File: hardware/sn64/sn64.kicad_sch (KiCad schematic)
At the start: 2 parts, among them J1 N64_Cartridge_Edge_50, J2 SNES_Female_Slot_62

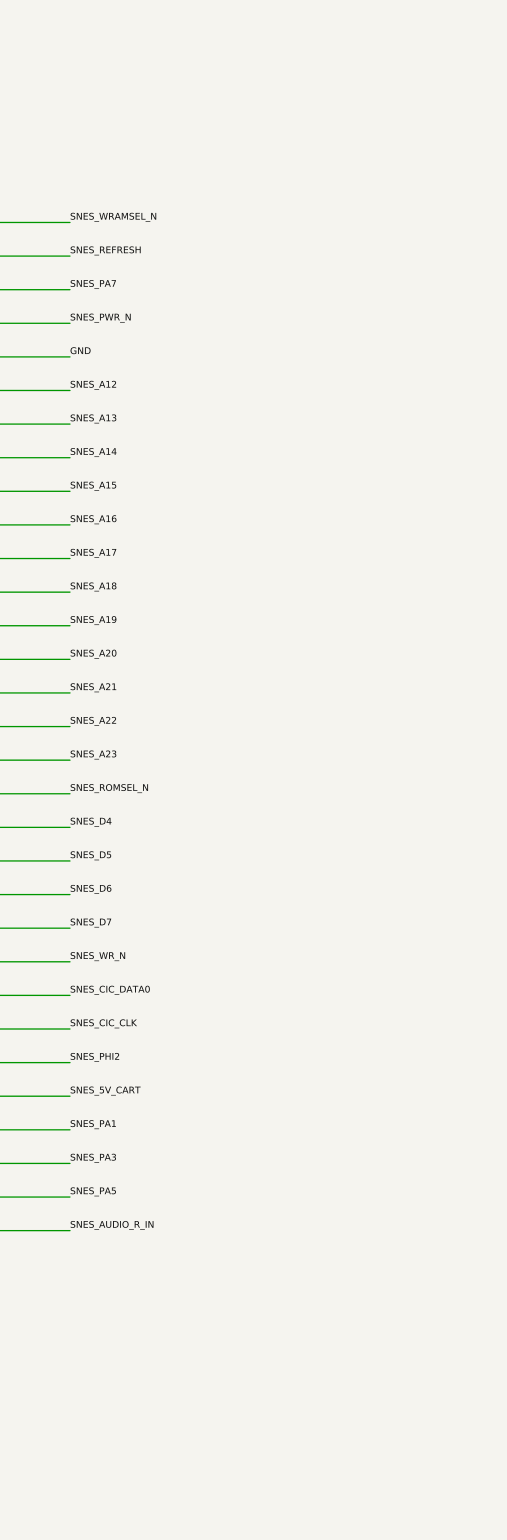
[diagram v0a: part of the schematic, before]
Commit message: Add SNES cartridge-interface schematic sheet
New KiCad child sheet with seven SN74LVC4245A translators (5 V cartridge
side, 3.3 V FPGA side): five fixed-direction octets for address, B-bus and
strobes on the bridge's shared enable, one octet for SYSTEM_CLK and the
CIC outputs on its own enable, and D0-D7 with FPGA-controlled direction
and enable. Every enable and the data DIR are pulled to cartridge 5 V and
pulled low only through 3.3 V open-drain buffers, so an unconfigured FPGA
or a missing interface rail leaves all translators disabled and no 5 V
pull-up reaches an FPGA pin. Adds the /RESET sink transistor, a 5 V
tolerant sense buffer, 33 R series arrays, bias and decoupling.

verify_cart_interface.py accounts for all 62 J2 contacts (17 checks) and
rejects two injected wiring faults. verify_interfaces.py now checks power
domain separation on connector pins only, since the translators
legitimately join the cartridge 5 V rail; all three validators pass
(30, 64, 17) and ERC has 0 errors.

Review finding recorded as must-fix before layout: CIC_DATA0/1 need
per-pin bidirectional drive; the lock protocol swaps the driver between
rounds. sn64_top gains snes_cic_oe_n for the CIC output octet.

Co-Authored-By: Claude Fable 5.1 <noreply@anthropic.com>
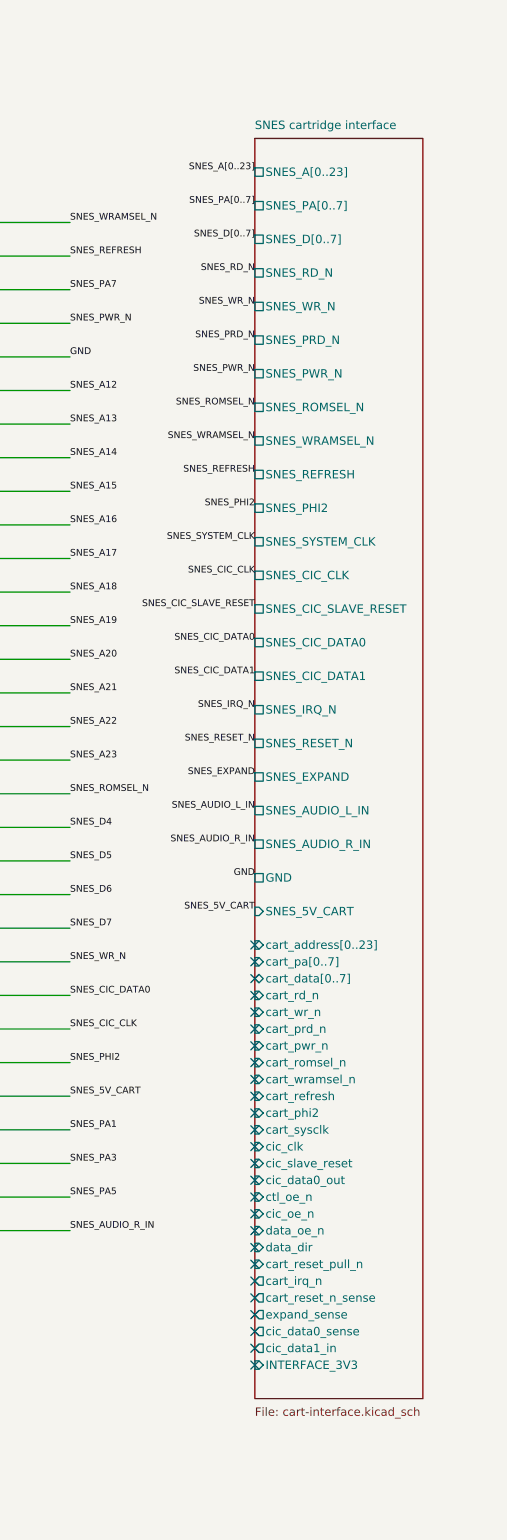
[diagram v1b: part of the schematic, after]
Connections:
- no-connect marks 0 -> 26
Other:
- added sheet SNES cartridge interface (cart-interface.kicad_sch)
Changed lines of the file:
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@@
 (sheet (at 20.32 229.87) (size 76.2 12.7) (stroke (width 0.1524) (type solid)) (fill (color 0 0 0 0)) (property "Sheetname" "USB-C programmer" (at 20.32 227.33 0) (effects (font (size 1.27 1.27)) (justify left)))(property "Sheetfile" "usb-programmer.kicad_sch" (at 20.32 245.11 0) (effects (font (size 1.27 1.27)) (justify left))) (pin "GND" passive (at 96.52 236.22 0) (effects (font (size 1.27 1.27)) (justify right))) (instances (project "sn64" (path "/e2505a21-9627-547b-aef4-ab0d2c57bd10" (page "2")))))
 (label "GND" (at 96.52 236.22 0) (effects (font (size 1.016 1.016)) (justify left bottom)))
+(sheet (at 375.92 38.1) (size 25.4 190.5) (stroke (width 0.1524) (type solid)) (fill (color 0 0 0 0)) (property "Sheetname" "SNES cartridge interface" (at 375.92 36.83 0) (effects (font (size 1.27 1.27)) (justify left bottom)))(property "Sheetfile" "cart-interface.kicad_sch" (at 375.92 229.87 0) (effects (font (size 1.27 1.27)) (justify left top))) (pin "SNES_A[0..23]" passive (at 375.92 43.18 180) (effects (font (size 1.27 1.27)) (justify left))) (pin "SNES_PA[0..7]" passive (at 375.92 48.26 180) (effects (font (size 1.27 1.27)) (justify left))) (pin "SNES_D[0..7]" passive (at 375.92 53.34 180) (effects (font (size 1.27 1.27)) (justify left))) (pin "SNES_RD_N" passive (at 375.92 58.42 180) (effects (font (size 1.27 1.27)) (justify left))) (pin "SNES_WR_N" passive (at 375.92 63.5 180) (effects (font (size 1.27 1.27)) (justify left))) (pin "SNES_PRD_N" passive (at 375.92 68.58 180) (effects (font (size 1.27 1.27)) (justify left))) (pin "SNES_PWR_N" passive (at 375.92 73.66 180) (effects (font (size 1.27 1.27)) (justify left))) (pin "SNES_ROMSEL_N" passive (at 375.92 78.74 180) (effects (font (size 1.27 1.27)) (justify left))) (pin "SNES_WRAMSEL_N" passive (at 375.92 83.82 180) (effects (font (size 1.27 1.27)) (justify left))) (pin "SNES_REFRESH" passive (at 375.92 88.9 180) (effects (font (size 1.27 1.27)) (justify left))) (pin "SNES_PHI2" passive (at 375.92 93.98 180) (effects (font (size 1.27 1.27)) (justify left))) (pin "SNES_SYSTEM_CLK" passive (at 375.92 99.06 180) (effects (font (size 1.27 1.27)) (justify left))) (pin "SNES_CIC_CLK" passive (at 375.92 104.14 180) (effects (font (size 1.27 1.27)) (justify left))) (pin "SNES_CIC_SLAVE_RESET" passive (at 375.92 109.22 180) (effects (font (size 1.27 1.27)) (justify left))) (pin "SNES_CIC_DATA0" passive (at 375.92 114.3 180) (effects (font (size 1.27 1.27)) (justify left))) (pin "SNES_CIC_DATA1" passive (at 375.92 119.38 180) (effects (font (size 1.27 1.27)) (justify left))) (pin "SNES_IRQ_N" passive (at 375.92 124.46 180) (effects (font (size 1.27 1.27)) (justify left))) (pin "SNES_RESET_N" passive (at 375.92 129.54 180) (effects (font (size 1.27 1.27)) (justify left))) (pin "SNES_EXPAND" passive (at 375.92 134.62 180) (effects (font (size 1.27 1.27)) (justify left))) (pin "SNES_AUDIO_L_IN" passive (at 375.92 139.7 180) (effects (font (size 1.27 1.27)) (justify left))) (pin "SNES_AUDIO_R_IN" passive (at 375.92 144.78 180) (effects (font (size 1.27 1.27)) (justify left))) (pin "GND" passive (at 375.92 149.86 180) (effects (font (size 1.27 1.27)) (justify left))) (pin "SNES_5V_CART" input (at 375.92 154.94 180) (effects (font (size 1.27 1.27)) (justify left))) (pin "cart_address[0..23]" input (at 375.92 160.02 180) (effects (font (size 1.27 1.27)) (justify left))) (pin "cart_pa[0..7]" input (at 375.92 162.56 180) (effects (font (size 1.27 1.27)) (justify left))) (pin "cart_data[0..7]" bidirectional (at 375.92 165.1 180) (effects (font (size 1.27 1.27)) (justify left))) (pin "cart_rd_n" input (at 375.92 167.64 180) (effects (font (size 1.27 1.27)) (justify left))) (pin "cart_wr_n" input (at 375.92 170.18 180) (effects (font (size 1.27 1.27)) (justify left))) (pin "cart_prd_n" input (at 375.92 172.72 180) (effects (font (size 1.27 1.27)) (justify left))) (pin "cart_pwr_n" input (at 375.92 175.26 180) (effects (font (size 1.27 1.27)) (justify left))) (pin "cart_romsel_n" input (at 375.92 177.8 180) (effects (font (size 1.27 1.27)) (justify left))) (pin "cart_wramsel_n" input (at 375.92 180.34 180) (effects (font (size 1.27 1.27)) (justify left))) (pin "cart_refresh" input (at 375.92 182.88 180) (effects (font (size 1.27 1.27)) (justify left))) (pin "cart_phi2" input (at 375.92 185.42 180) (effects (font (size 1.27 1.27)) (justify left))) (pin "cart_sysclk" input (at 375.92 187.96 180) (effects (font (size 1.27 1.27)) (justify left))) (pin "cic_clk" input (at 375.92 190.5 180) (effects (font (size 1.27 1.27)) (justify left))) (pin "cic_slave_reset" input (at 375.92 193.04 180) (effects (font (size 1.27 1.27)) (justify left))) (pin "cic_data0_out" input (at 375.92 195.58 180) (effects (font (size 1.27 1.27)) (justify left))) (pin "ctl_oe_n" input (at 375.92 198.12 180) (effects (font (size 1.27 1.27)) (justify left))) (pin "cic_oe_n" input (at 375.92 200.66 180) (effects (font (size 1.27 1.27)) (justify left))) (pin "data_oe_n" input (at 375.92 203.2 180) (effects (font (size 1.27 1.27)) (justify left))) (pin "data_dir" input (at 375.92 205.74 180) (effects (font (size 1.27 1.27)) (justify left))) (pin "cart_reset_pull_n" input (at 375.92 208.28 180) (effects (font (size 1.27 1.27)) (justify left))) (pin "cart_irq_n" output (at 375.92 210.82 180) (effects (font (size 1.27 1.27)) (justify left))) (pin "cart_reset_n_sense" output (at 375.92 213.36 180) (effects (font (size 1.27 1.27)) (justify left))) (pin "expand_sense" output (at 375.92 215.9 180) (effects (font (size 1.27 1.27)) (justify left))) (pin "cic_data0_sense" output (at 375.92 218.44 180) (effects (font (size 1.27 1.27)) (justify left))) (pin "cic_data1_in" output (at 375.92 220.98 180) (effects (font (size 1.27 1.27)) (justify left))) (pin "INTERFACE_3V3" input (at 375.92 223.52 180) (effects (font (size 1.27 1.27)) (justify left))) (instances (project "sn64" (path "/e2505a21-9627-547b-aef4-ab0d2c57bd10" (page "3")))))
+(label "SNES_A[0..23]" (at 375.92 43.18 180) (effects (font (size 1.016 1.016)) (justify right bottom)))
+(label "SNES_PA[0..7]" (at 375.92 48.26 180) (effects (font (size 1.016 1.016)) (justify right bottom)))
+(label "SNES_D[0..7]" (at 375.92 53.34 180) (effects (font (size 1.016 1.016)) (justify right bottom)))
+(label "SNES_RD_N" (at 375.92 58.42 180) (effects (font (size 1.016 1.016)) (justify right bottom)))
+(label "SNES_WR_N" (at 375.92 63.5 180) (effects (font (size 1.016 1.016)) (justify right bottom)))
+(label "SNES_PRD_N" (at 375.92 68.58 180) (effects (font (size 1.016 1.016)) (justify right bottom)))
+(label "SNES_PWR_N" (at 375.92 73.66 180) (effects (font (size 1.016 1.016)) (justify right bottom)))
+(label "SNES_ROMSEL_N" (at 375.92 78.74 180) (effects (font (size 1.016 1.016)) (justify right bottom)))
+(label "SNES_WRAMSEL_N" (at 375.92 83.82 180) (effects (font (size 1.016 1.016)) (justify right bottom)))
+(label "SNES_REFRESH" (at 375.92 88.9 180) (effects (font (size 1.016 1.016)) (justify right bottom)))
+(label "SNES_PHI2" (at 375.92 93.98 180) (effects (font (size 1.016 1.016)) (justify right bottom)))
+(label "SNES_SYSTEM_CLK" (at 375.92 99.06 180) (effects (font (size 1.016 1.016)) (justify right bottom)))
+(label "SNES_CIC_CLK" (at 375.92 104.14 180) (effects (font (size 1.016 1.016)) (justify right bottom)))
+(label "SNES_CIC_SLAVE_RESET" (at 375.92 109.22 180) (effects (font (size 1.016 1.016)) (justify right bottom)))
+(label "SNES_CIC_DATA0" (at 375.92 114.3 180) (effects (font (size 1.016 1.016)) (justify right bottom)))
+(label "SNES_CIC_DATA1" (at 375.92 119.38 180) (effects (font (size 1.016 1.016)) (justify right bottom)))
+(label "SNES_IRQ_N" (at 375.92 124.46 180) (effects (font (size 1.016 1.016)) (justify right bottom)))
+(label "SNES_RESET_N" (at 375.92 129.54 180) (effects (font (size 1.016 1.016)) (justify right bottom)))
+(label "SNES_EXPAND" (at 375.92 134.62 180) (effects (font (size 1.016 1.016)) (justify right bottom)))
+(label "SNES_AUDIO_L_IN" (at 375.92 139.7 180) (effects (font (size 1.016 1.016)) (justify right bottom)))
+(label "SNES_AUDIO_R_IN" (at 375.92 144.78 180) (effects (font (size 1.016 1.016)) (justify right bottom)))
+(label "GND" (at 375.92 149.86 180) (effects (font (size 1.016 1.016)) (justify right bottom)))
+(label "SNES_5V_CART" (at 375.92 154.94 180) (effects (font (size 1.016 1.016)) (justify right bottom)))
+(no_connect (at 375.92 160.02))
+(no_connect (at 375.92 162.56))
+(no_connect (at 375.92 165.1))
+(no_connect (at 375.92 167.64))
+(no_connect (at 375.92 170.18))
+(no_connect (at 375.92 172.72))
+(no_connect (at 375.92 175.26))
+(no_connect (at 375.92 177.8))
+(no_connect (at 375.92 180.34))
+(no_connect (at 375.92 182.88))
+(no_connect (at 375.92 185.42))
+(no_connect (at 375.92 187.96))
+(no_connect (at 375.92 190.5))
+(no_connect (at 375.92 193.04))
+(no_connect (at 375.92 195.58))
+(no_connect (at 375.92 198.12))
+(no_connect (at 375.92 200.66))
+(no_connect (at 375.92 203.2))
+(no_connect (at 375.92 205.74))
+(no_connect (at 375.92 208.28))
+(no_connect (at 375.92 210.82))
+(no_connect (at 375.92 213.36))
+(no_connect (at 375.92 215.9))
+(no_connect (at 375.92 218.44))
+(no_connect (at 375.92 220.98))
+(no_connect (at 375.92 223.52))
 )
